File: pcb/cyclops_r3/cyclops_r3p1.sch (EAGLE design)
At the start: 50 parts, among them Q1 SUM11006, Q2 IRF510, U1 MCP4921, U2 317-N, U3 ADR03, U4 OP1177, U5 LM324N, U6 ZXTD45

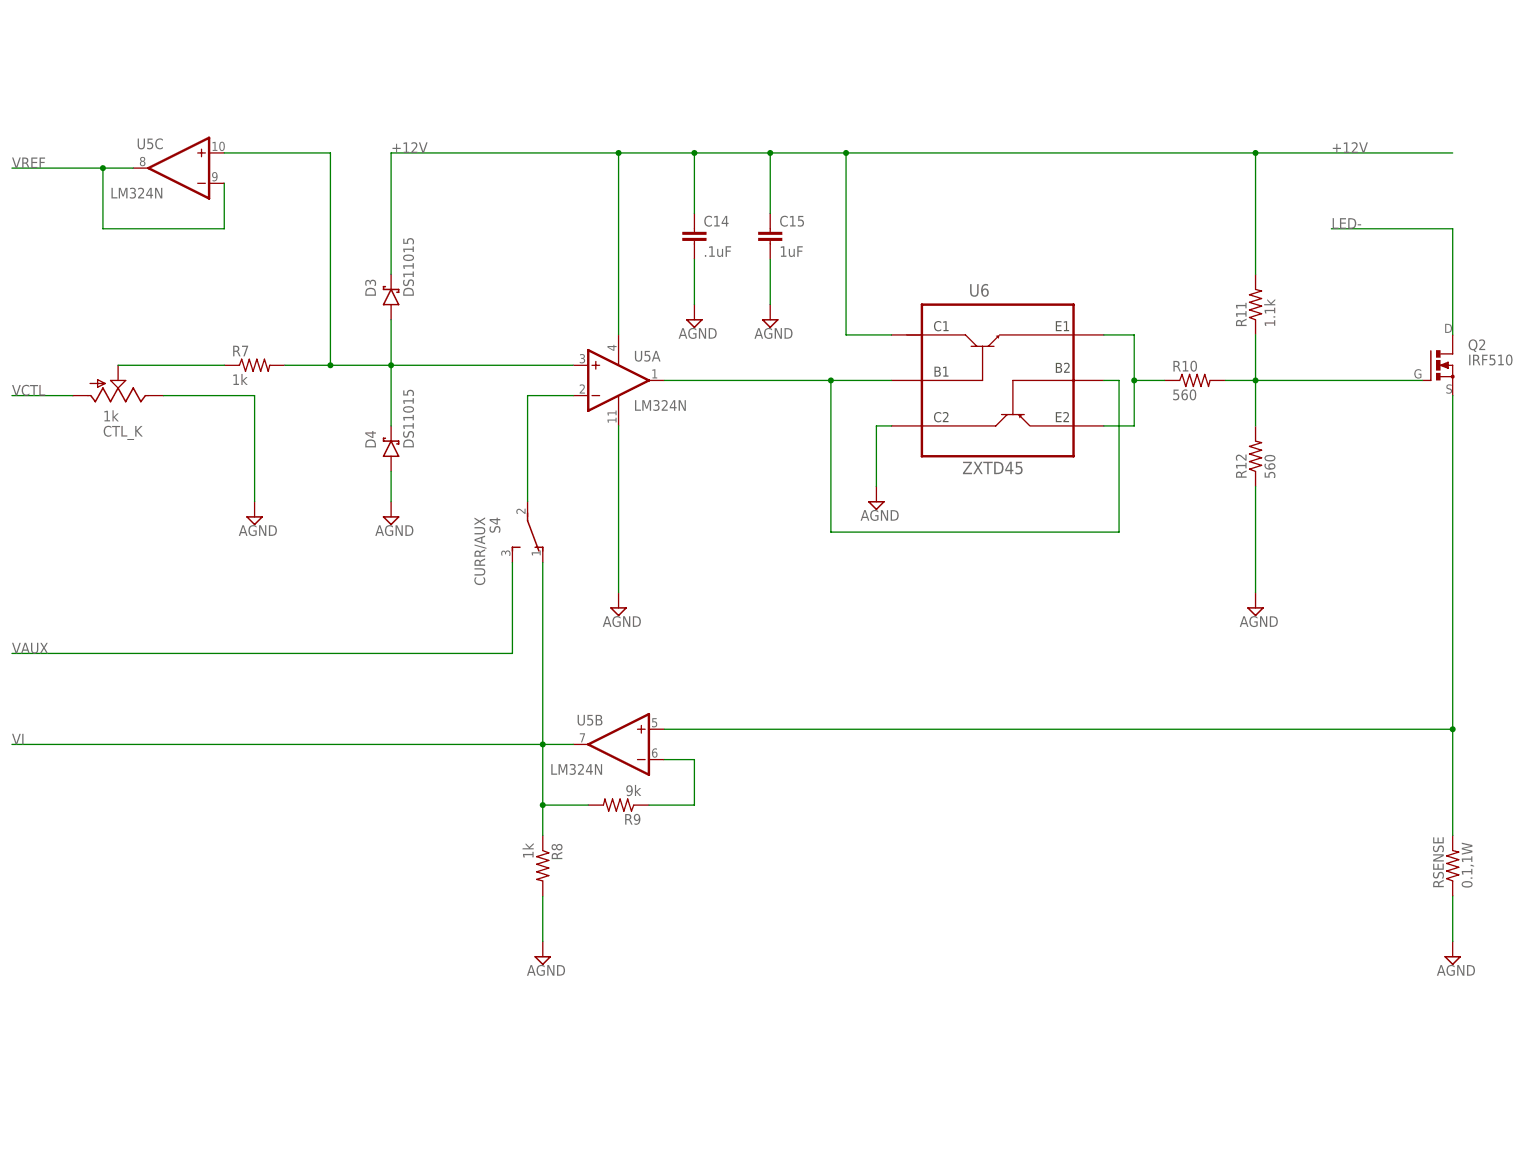
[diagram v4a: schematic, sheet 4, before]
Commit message: Put the circuit on the breadboard today and found several mistakes/improvments to the design. I implemented some of those here and documented what else needs to be done in the notes.
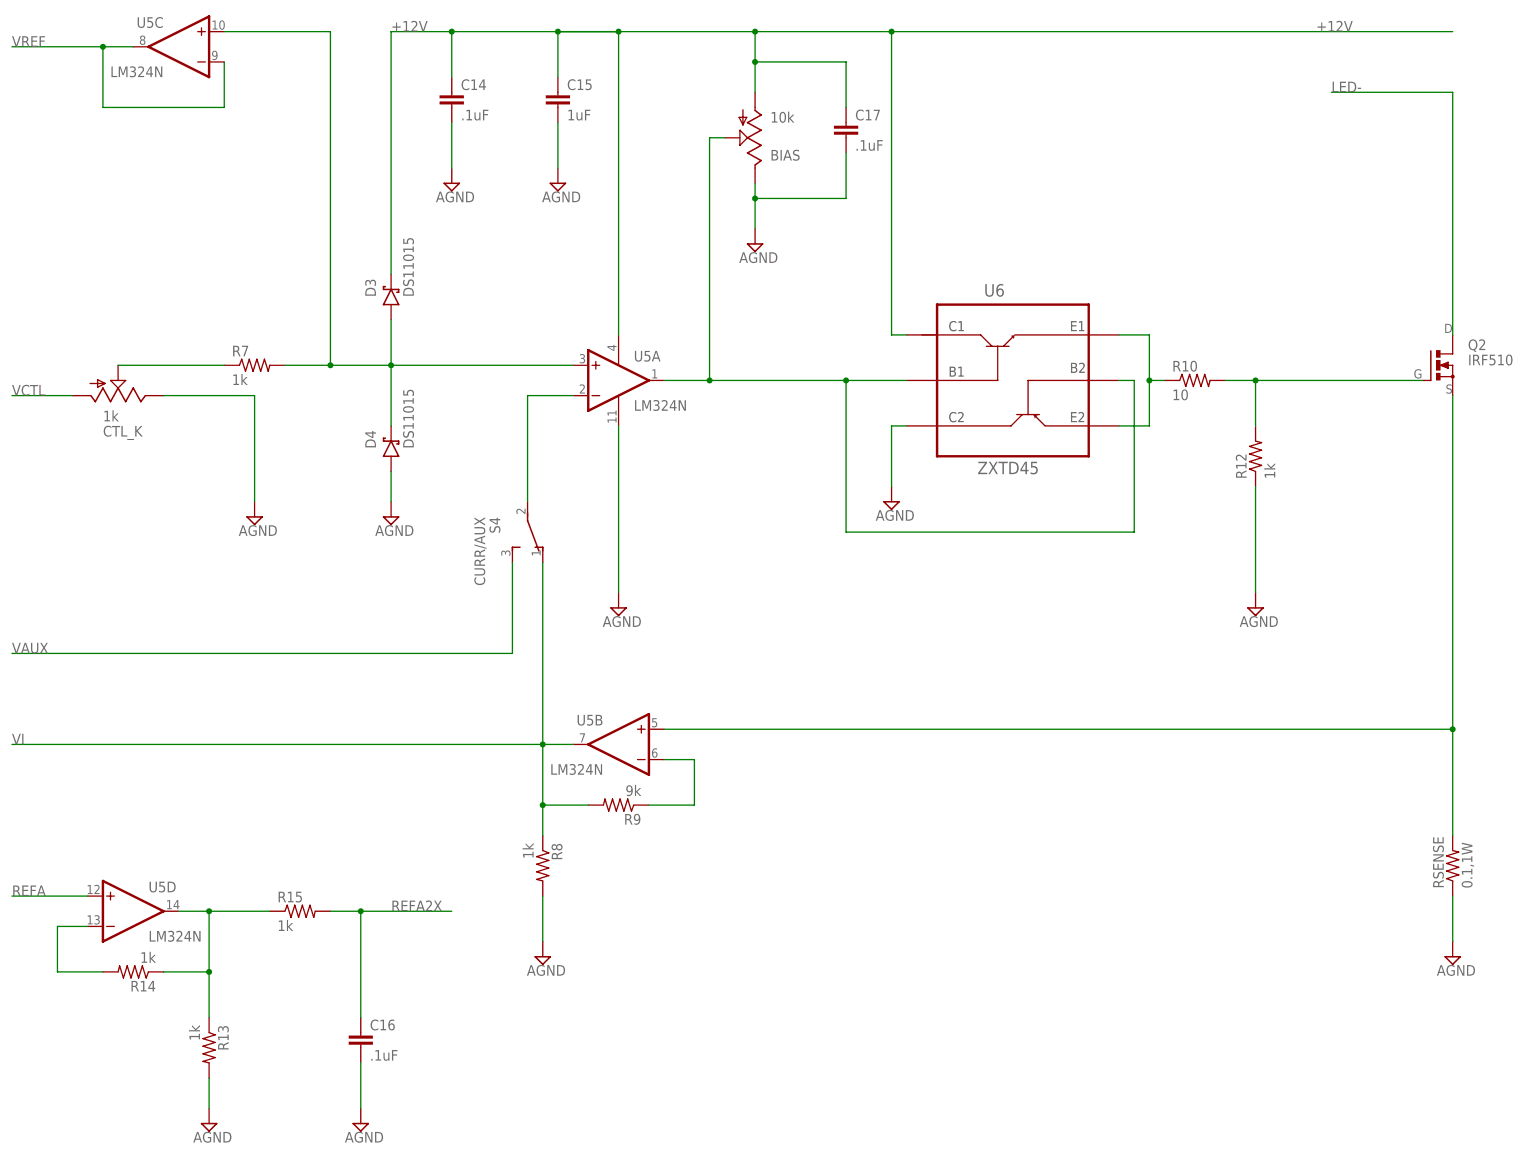
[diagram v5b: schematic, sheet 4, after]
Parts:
- removed R11: 1.1k, cyclops:R_0603
- added BIAS: 10k, cyclops:TRIM_US-SM-42/43W
- added C16, C17: .1uF, cyclops:C_0603
- added R13, R14, R15: 1k, cyclops:R_0603
- R10: value 560 -> 10
- R12: value 560 -> 1k
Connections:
- net _VCTL renamed VCTL_PRE
- removed net N$3: U5A.OUT, U6.B1, U6.B2
- new net AGND: BIAS.E, C17.2
- new net N$4: BIAS.S, U5A.OUT, U6.B1, U6.B2
- new net N$8: R14.2, U5D.-IN
- new net REFA2X: C16.1, R15.2, S3.3
- new net VREFA2X: R13.1, R14.1, R15.1, U5D.OUT
- net +12V: now also BIAS.A, C17.1; no longer R11.2
- net GND: now also C16.2, R13.2
- net N$13: no longer R11.1
- net REFA: now also U5D.+IN; no longer S3.3
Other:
- moved on the sheet: C14, C15, C6, R3, U5C, U6

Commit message: Added some test points to the the circuit and a design note.
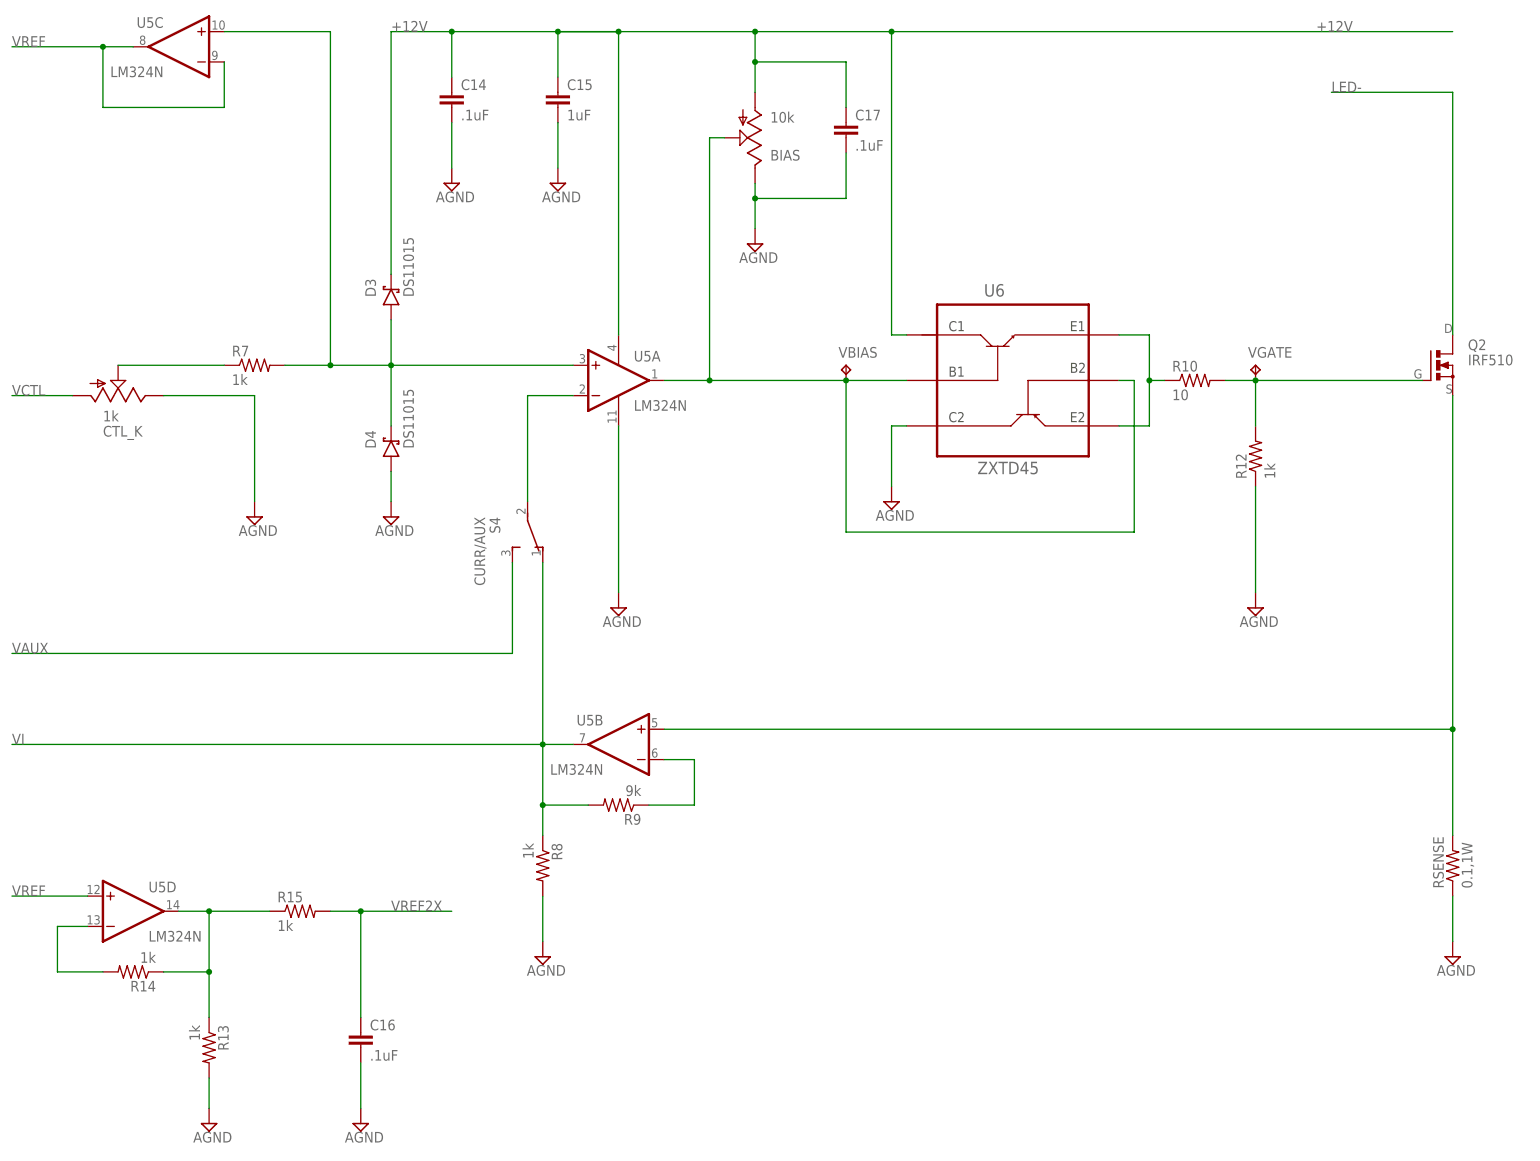
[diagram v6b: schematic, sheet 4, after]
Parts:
- added VBIAS, VGATE, VREF, VTEMP: TPTP08R, cyclops:TPTP08R
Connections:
- net REFA2X renamed VREF2X
- removed net REFA: C2.1, REF_ADJ.A, U1.REFA, U3.VOUT, U5D.+IN
- net N$13: now also VGATE.TP
- net N$4: now also VBIAS.TP
- net VREF: now also C2.1, REF_ADJ.A, U1.REFA, U3.VOUT, U5D.+IN, VREF.TP
- net VTEMP: now also VTEMP.TP
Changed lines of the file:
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@@
 <part name="SUPPLY39" library="cyclops" deviceset="AGND" device=""/>
 <part name="C17" library="cyclops" deviceset="C" device="_0603" value=".1uF"/>
+<part name="VREF" library="cyclops" deviceset="TP" device="TP08R"/>
+<part name="VTEMP" library="cyclops" deviceset="TP" device="TP08R"/>
+<part name="VBIAS" library="cyclops" deviceset="TP" device="TP08R"/>
+<part name="VGATE" library="cyclops" deviceset="TP" device="TP08R"/>
 </parts>
 <sheets>
@@
 </segment>
 </net>
-<net name="REFA" class="0">
-<segment>
-<pinref part="U1" gate="G$1" pin="REFA"/>
-<wire x1="180.34" y1="53.34" x2="205.74" y2="53.34" width="0.1524" layer="91"/>
-<label x="193.04" y="53.34" size="1.778" layer="95"/>
-<pinref part="C2" gate="C" pin="1"/>
-<wire x1="205.74" y1="45.72" x2="205.74" y2="53.34" width="0.1524" layer="91"/>
-</segment>
-</net>
 <net name="DACA" class="0">
 <segment>
@@
 <label x="50.8" y="-30.48" size="1.778" layer="95"/>
 </segment>
+<segment>
+<pinref part="U1" gate="G$1" pin="REFA"/>
+<wire x1="180.34" y1="53.34" x2="205.74" y2="53.34" width="0.1524" layer="91"/>
+<label x="193.04" y="53.34" size="1.778" layer="95"/>
+<pinref part="C2" gate="C" pin="1"/>
+<wire x1="205.74" y1="45.72" x2="205.74" y2="53.34" width="0.1524" layer="91"/>
+</segment>
 </net>
 <net name="VTEMP" class="0">
@@
 </segment>
 </net>
-<net name="REFA2X" class="0">
+<net name="VREF2X" class="0">
 <segment>
 <pinref part="S3" gate="G$1" pin="3"/>
@@
 <instance part="C13" gate="C" x="-58.42" y="-106.68"/>
 <instance part="C11" gate="C" x="-73.66" y="-106.68"/>
+<instance part="VREF" gate="G$1" x="35.56" y="5.08"/>
+<instance part="VTEMP" gate="G$1" x="35.56" y="-81.28"/>
 </instances>
 <busses>
@@
 </segment>
 </net>
-<net name="REFA" class="0">
+<net name="VREF" class="0">
 <segment>
 <wire x1="17.78" y1="2.54" x2="35.56" y2="2.54" width="0.1524" layer="91"/>
@@
 <junction x="35.56" y="2.54"/>
 <label x="53.34" y="2.54" size="1.778" layer="95"/>
+<pinref part="VREF" gate="G$1" pin="TP"/>
 </segment>
 </net>
@@
 <junction x="35.56" y="-83.82"/>
 <label x="50.8" y="-83.82" size="1.778" layer="95"/>
+<pinref part="VTEMP" gate="G$1" pin="TP"/>
 </segment>
 </net>
@@
 <instance part="SUPPLY39" gate="G$1" x="50.8" y="106.68"/>
 <instance part="C17" gate="C" x="66.04" y="127"/>
+<instance part="VBIAS" gate="G$1" x="66.04" y="86.36"/>
+<instance part="VGATE" gate="G$1" x="134.62" y="86.36"/>
 </instances>
 <busses>
@@
 <pinref part="U5" gate="C" pin="OUT"/>
 <label x="-73.66" y="139.7" size="1.778" layer="95"/>
+</segment>
+<segment>
+<pinref part="U5" gate="D" pin="+IN"/>
+<wire x1="-73.66" y1="-2.54" x2="-60.96" y2="-2.54" width="0.1524" layer="91"/>
+<label x="-73.66" y="-2.54" size="1.778" layer="95"/>
 </segment>
 </net>
@@
 <pinref part="R12" gate="R" pin="2"/>
 <wire x1="134.62" y1="83.82" x2="134.62" y2="76.2" width="0.1524" layer="91"/>
+<pinref part="VGATE" gate="G$1" pin="TP"/>
 </segment>
 </net>
@@
 <wire x1="167.64" y1="132.08" x2="147.32" y2="132.08" width="0.1524" layer="91"/>
 <label x="147.32" y="132.08" size="1.778" layer="95"/>
-</segment>
-</net>
-<net name="REFA" class="0">
-<segment>
-<pinref part="U5" gate="D" pin="+IN"/>
-<wire x1="-73.66" y1="-2.54" x2="-60.96" y2="-2.54" width="0.1524" layer="91"/>
-<label x="-73.66" y="-2.54" size="1.778" layer="95"/>
 </segment>
 </net>
@@
 </segment>
 </net>
-<net name="REFA2X" class="0">
+<net name="VREF2X" class="0">
 <segment>
 <pinref part="R15" gate="R" pin="2"/>
@@
 <junction x="43.18" y="83.82"/>
 <junction x="66.04" y="83.82"/>
-</segment>
-</net>
+<pinref part="VBIAS" gate="G$1" pin="TP"/>
+</segment>
+</net>
